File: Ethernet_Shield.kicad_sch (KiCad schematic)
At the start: 44 parts, among them J10 RJ45_Abracon_ARJP11A-MASA-B-A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, U1 AP2127K-3.3, U2 W5500, Y1 25Mhz

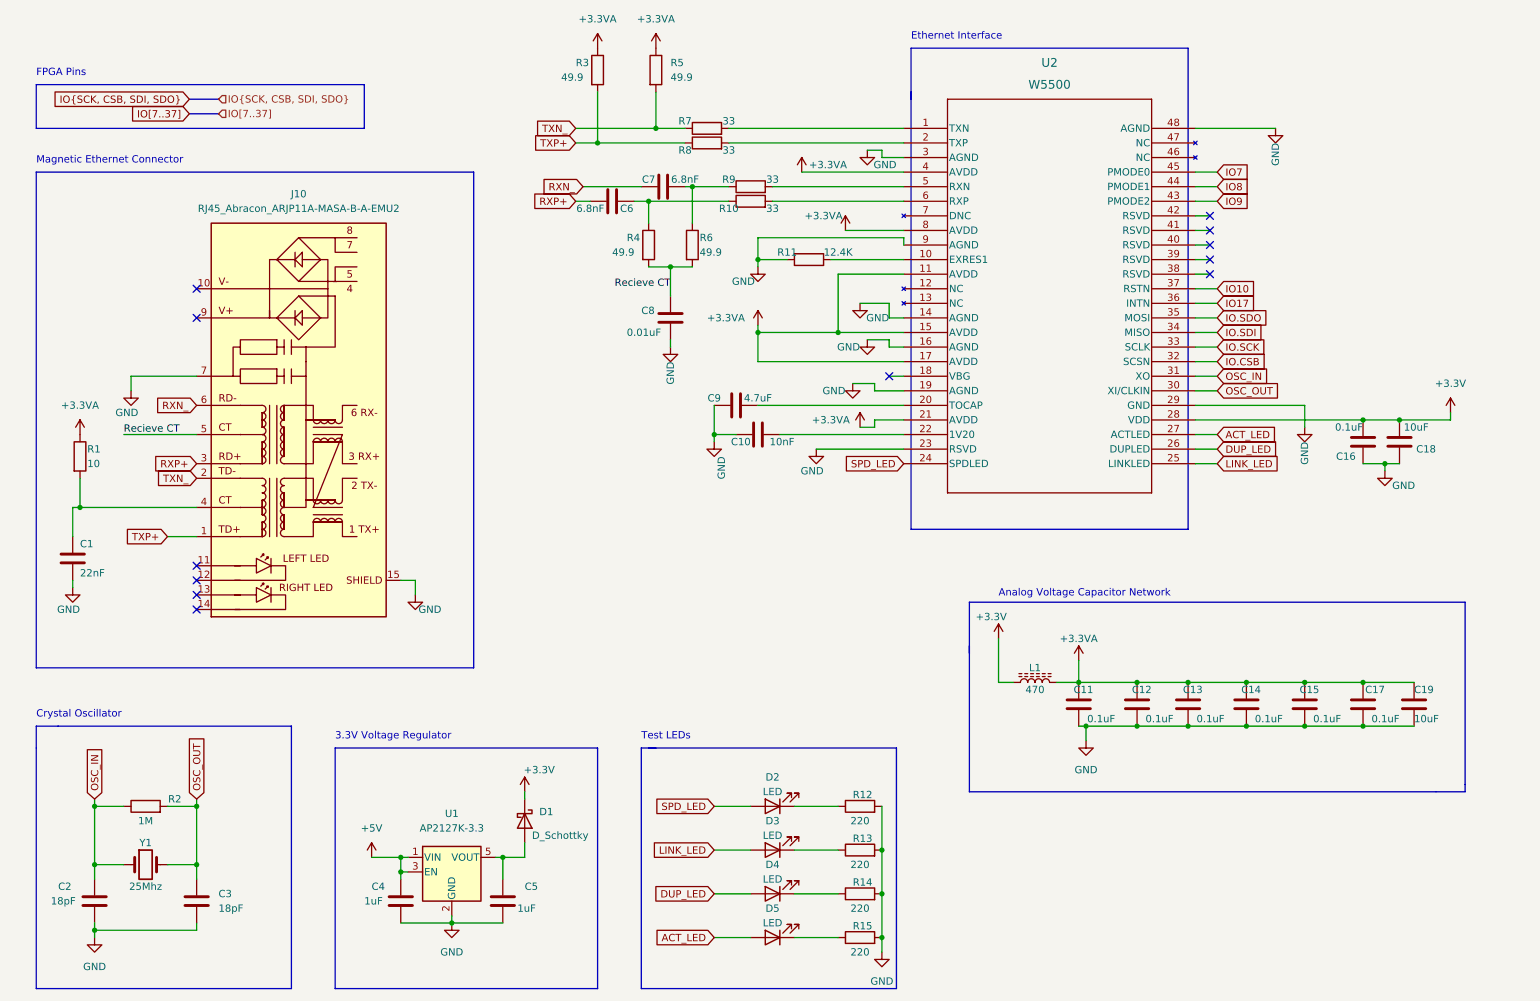
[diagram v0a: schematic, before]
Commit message: Fixed Schematic with LDR, Capacitor Network, and magnetic RJ45. Re-did the PCB layout
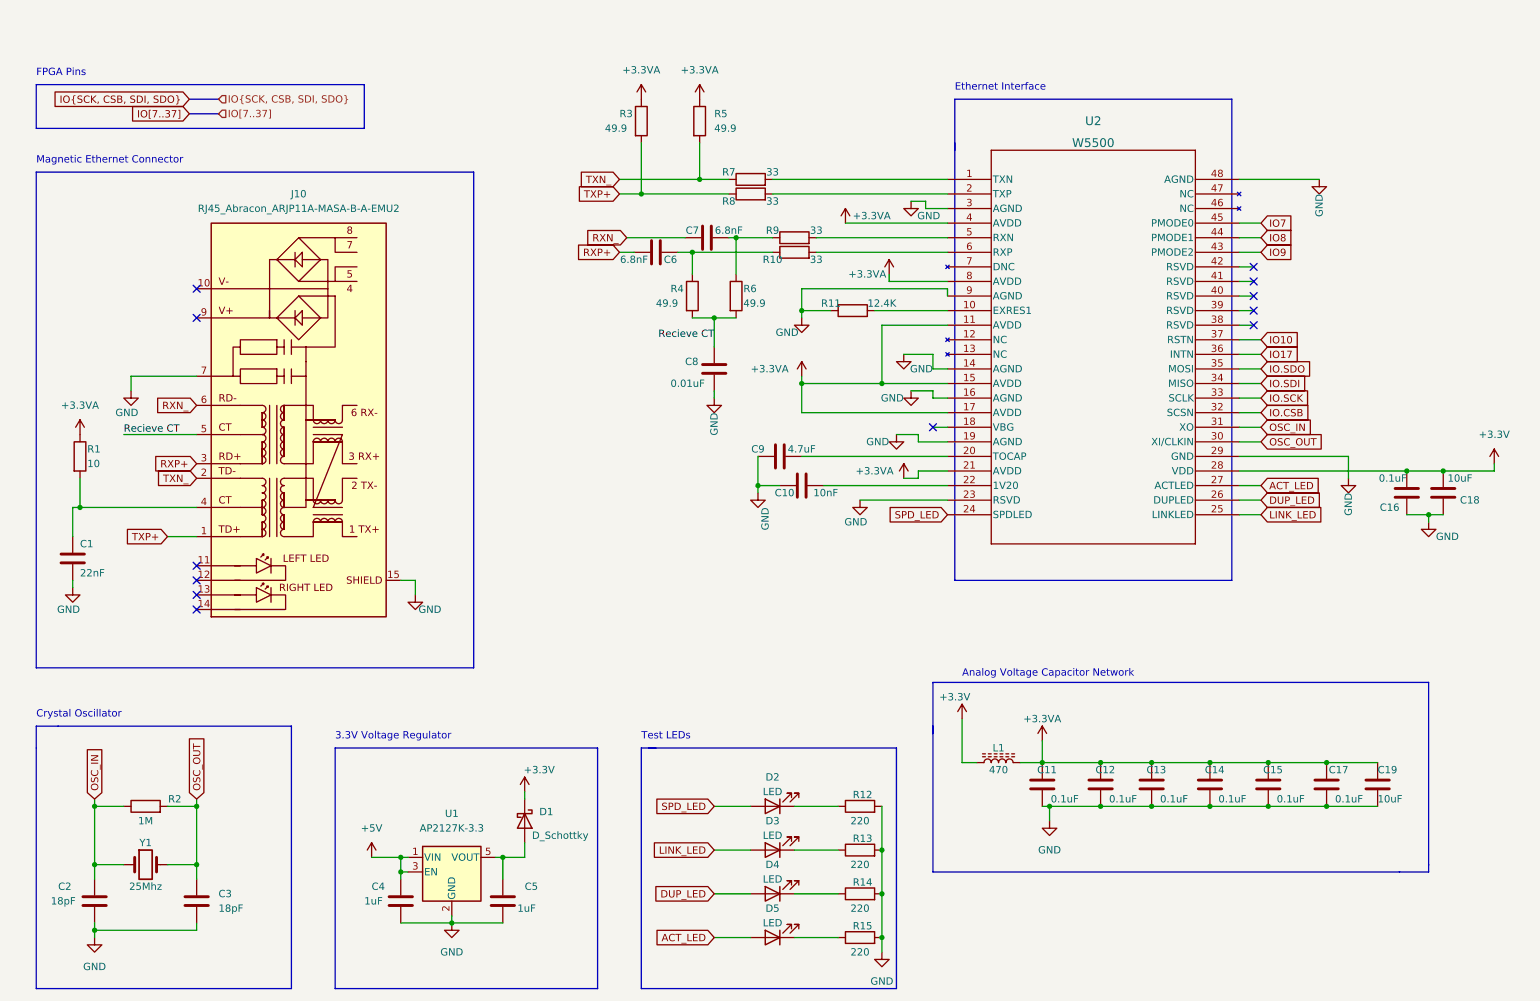
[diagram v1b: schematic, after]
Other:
- moved on the sheet: C10, C11, C12, C13, C14, C15, C16, C17, C18, C19, C6, C7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

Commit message: Revised schematic. Re-did Board to 2 Layers
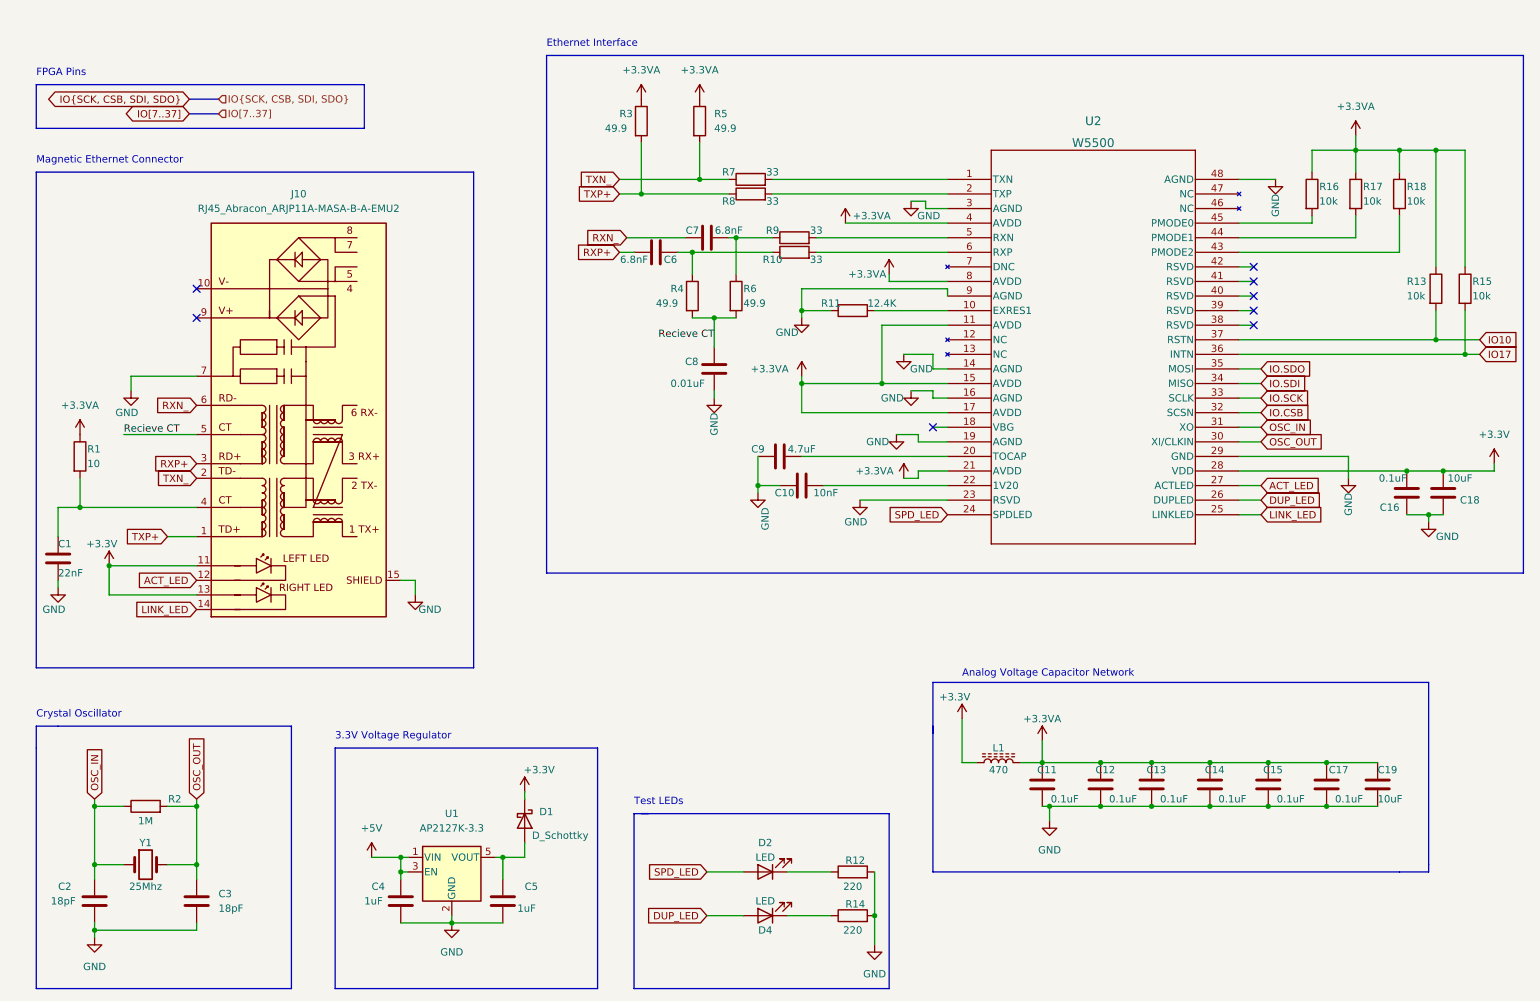
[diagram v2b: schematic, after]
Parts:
- removed D3, D5: LED, LED_SMD:LED_1206_3216Metric, symbol Device:LED
- added R16, R17, R18: 10k, Resistor_SMD:R_1206_3216Metric, symbol Device:R
- R13, R15: value 220 -> 10k
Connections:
- net +3.3V: now also J10.11 (LLED+), J10.13 (RLED+)
- net +3.3VA: now also R13.1, R15.1, R16.1, R17.1, R18.1
- net ACT_LED: now also J10.12 (LLED-)
- net GND: no longer R13.2, R15.2
- net IO10: now also R13.2
- net IO17: now also R15.2
- net LINK_LED: now also J10.14 (RLED-)
- net IO7: no longer names the net of U2.45 (PMODE0)
- net IO7: now also R16.2
- net IO8: no longer names the net of U2.44 (PMODE1)
- net IO8: now also R17.2
- net IO9: no longer names the net of U2.43 (PMODE2)
- net IO9: now also R18.2
- no-connect marks 12 -> 8
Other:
- moved on the sheet: C1, D2, D4, R12, R14
